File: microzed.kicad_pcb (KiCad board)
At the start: 10 copper layers, 50 x 100 mm, 334 parts, among them IC1 XC7Z020-1CLG484C, IC2 RTL8211E-VL-CG, J1 640456-3, J2 10104111-0001LF, J3 L829-1J1T-43, J4 Micro_SD_Card_Det_Hirose_DM3AT, J5 10104111-0001LF, J6 BSH-090-01-X-D-A, J7 BSH-090-01-X-D-A, Q1 MMBT3904, Q2 MMBT3904, SW1 SW_Push, U1 TLV62130RGTR, U10 MT41K256M16TW, U11 MT25QL128ABA8E12-1SIT, U12 USB3320C-EZK, U13 ASDMB-24.000MHZ-LC-T, U14 ASDMB-25.000MHZ-LC-T, U15 TXS02612RTWR, U16 CP2104-F03-GM, U2 TLV62130RGTR, U3 TLV62130RGTR, U4 TLV62130RGTR, U5 TLV62130RGTR, U6 ASDMB-33.333MHZ-LC-T, U7 TPS51206DSQR, U8 REF3012, U9 MT41K256M16TW

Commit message: pcb: start memory.
Signed-off-by: Yi Qingliang <niqingliang2003@gmail.com>
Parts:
- moved IC1 1.30 mm to (0.00, 48.2)
- moved U10 1.30 mm to (-5.40, 29.6)
- moved U9 1.30 mm to (5.40, 29.6)
- moved J6 1.30 mm to (-18.4, 45.0)
- moved J7 1.30 mm to (18.4, 45.0)
- moved C131 0.92 mm to (-7.40, 20.6), turned to 180 degrees
- moved C102 0.72 mm to (7.40, 20.6)
- moved C104 0.63 mm to (3.40, 20.6), turned to 180 degrees
- moved C121 0.61 mm to (-3.40, 20.6)
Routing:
- net DDR3_RST#: track 0.00 -> 0.57 mm, vias 0 -> 1
- net VCCO_DDR: vias 7 -> 13
- added copper zone on In5.Cu.GND, net VCCO_DDR

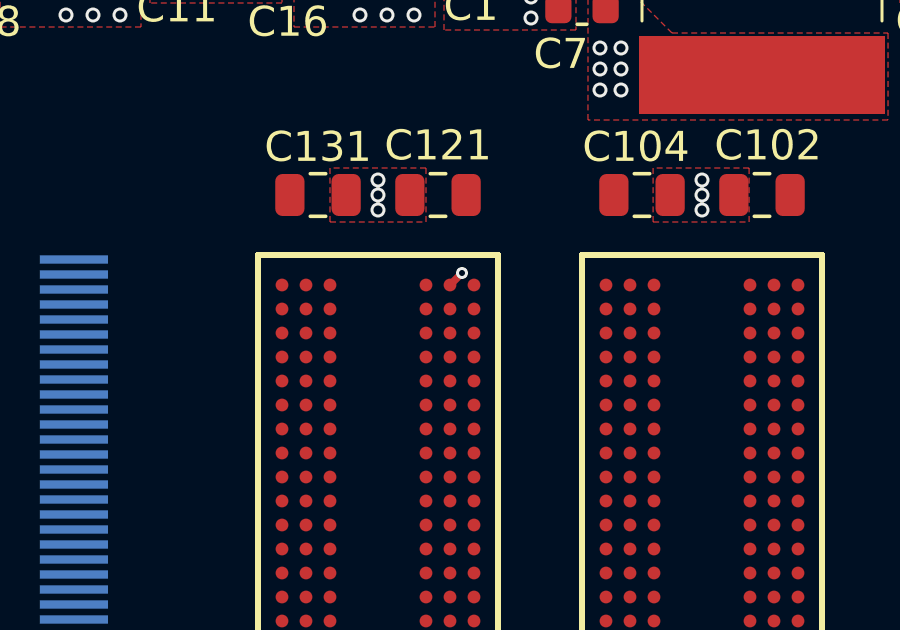
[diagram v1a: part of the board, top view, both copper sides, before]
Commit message: relax via settings
Signed-off-by: Yi Qingliang <niqingliang2003@gmail.com>
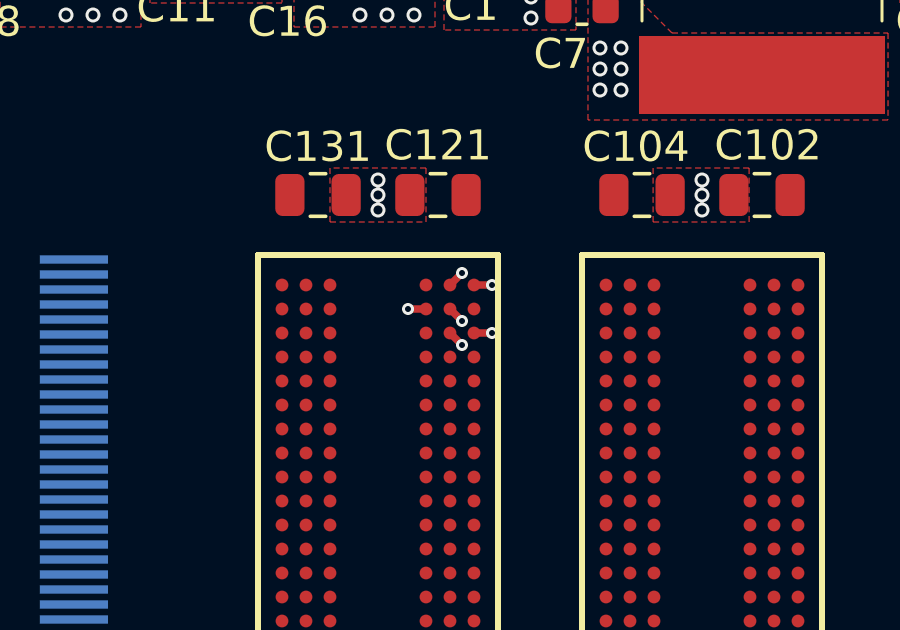
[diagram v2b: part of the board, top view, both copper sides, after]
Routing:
- net GND: track 16.4 -> 17.6 mm, vias 45 -> 47
- net DDR3_A9: track 0.00 -> 0.60 mm, vias 0 -> 1
- net DDR3_A7: track 0.00 -> 0.57 mm, vias 0 -> 1
- net DDR3_A5: track 0.00 -> 0.57 mm, vias 0 -> 1
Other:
- rule via_min_drill: 0.3 -> 0.2
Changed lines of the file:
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@@
     (thickness 1.6)
     (drawings 4)
-    (tracks 242)
+    (tracks 257)
     (zones 0)
     (modules 334)
@@
     (via_drill 0.4)
     (via_min_size 0.4)
-    (via_min_drill 0.3)
+    (via_min_drill 0.2)
+    (user_via 0.4 0.2)
     (user_via 0.5 0.3)
     (uvia_size 0.3)
@@
   (gr_line (start -25 100) (end -25 0) (layer Edge.Cuts) (width 0.05))
   (gr_line (start 25 100) (end -25 100) (layer Edge.Cuts) (width 0.05))
+  (via (at -2.6 25.6) (size 0.4) (drill 0.2) (layers F.Cu B.Cu) (net 222))
+  (via (at -2.6 24.8) (size 0.4) (drill 0.2) (layers F.Cu B.Cu) (net 234))
   (via (at -2.6 23.2) (size 0.4) (drill 0.2) (layers F.Cu B.Cu) (net 282))
-  (via (at -5.4 20.6) (size 0.5) (drill 0.3) (layers F.Cu B.Cu) (net 10))
-  (via (at -5.4 20.1) (size 0.5) (drill 0.3) (layers F.Cu B.Cu) (net 10))
-  (via (at -5.4 21.1) (size 0.5) (drill 0.3) (layers F.Cu B.Cu) (net 10))
   (via (at -18.3 10.5) (size 0.5) (drill 0.3) (layers F.Cu B.Cu) (net 1))
   (via (at -19.3 10.5) (size 0.5) (drill 0.3) (layers F.Cu B.Cu) (net 1))
@@
   (via (at 1.3 9.5) (size 0.5) (drill 0.3) (layers F.Cu B.Cu) (net 1))
   (via (at 0.8 10) (size 0.5) (drill 0.3) (layers F.Cu B.Cu) (net 1))
+  (segment (start -2.2 23.6) (end -1.6 23.6) (width 0.25) (layer F.Cu) (net 1))
+  (segment (start -1.6 23.6) (end -1.6 23.6) (width 0.25) (layer F.Cu) (net 1))
+  (segment (start -1.6 23.6) (end -1.6 23.6) (width 0.25) (layer F.Cu) (net 1))
+  (segment (start -2.2 25.2) (end -1.6 25.2) (width 0.25) (layer F.Cu) (net 1))
+  (segment (start -1.6 25.2) (end -1.6 25.2) (width 0.25) (layer F.Cu) (net 1))
+  (via (at -1.6 25.2) (size 0.4) (drill 0.2) (layers F.Cu B.Cu) (net 1))
+  (segment (start -1.6 23.6) (end -1.6 23.6) (width 0.25) (layer F.Cu) (net 1))
+  (via (at -1.6 23.6) (size 0.4) (drill 0.2) (layers F.Cu B.Cu) (net 1))
   (via (at 13.4 10) (size 0.5) (drill 0.3) (layers F.Cu B.Cu) (net 2))
   (via (at 12.4 10) (size 0.5) (drill 0.3) (layers F.Cu B.Cu) (net 2))
@@
   (segment (start 15.75 11.4625) (end 15.75 11.975) (width 0.25) (layer F.Cu) (net 9))
   (segment (start 15.75 11.975) (end 16.075 12.3) (width 0.25) (layer F.Cu) (net 9))
+  (via (at -5.4 20.6) (size 0.5) (drill 0.3) (layers F.Cu B.Cu) (net 10))
+  (via (at -5.4 20.1) (size 0.5) (drill 0.3) (layers F.Cu B.Cu) (net 10))
+  (via (at -5.4 21.1) (size 0.5) (drill 0.3) (layers F.Cu B.Cu) (net 10))
   (via (at -4.2 13.7) (size 0.5) (drill 0.3) (layers F.Cu B.Cu) (net 10))
   (via (at -6 13.7) (size 0.5) (drill 0.3) (layers F.Cu B.Cu) (net 10))
@@
   (via (at 5.4 20.1) (size 0.5) (drill 0.3) (layers F.Cu B.Cu) (net 10))
   (via (at 5.4 21.1) (size 0.5) (drill 0.3) (layers F.Cu B.Cu) (net 10))
+  (segment (start -3 25.2) (end -2.6 25.6) (width 0.25) (layer F.Cu) (net 222))
+  (segment (start -2.6 24.8) (end -3 24.4) (width 0.25) (layer F.Cu) (net 234))
+  (segment (start -3.8 24.4) (end -4.4 24.4) (width 0.25) (layer F.Cu) (net 246))
+  (segment (start -4.4 24.4) (end -4.4 24.4) (width 0.25) (layer F.Cu) (net 246))
+  (via (at -4.4 24.4) (size 0.4) (drill 0.2) (layers F.Cu B.Cu) (net 246))
   (segment (start -3 23.6) (end -2.6 23.2) (width 0.25) (layer F.Cu) (net 282))
   (via (at 18.7 8.8) (size 0.5) (drill 0.3) (layers F.Cu B.Cu) (net 350))

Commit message: start DDR3 DQ[0-7]
Signed-off-by: Yi Qingliang <niqingliang2003@gmail.com>
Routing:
- net DDR3_DQS0_P: track 0.00 -> 12.9 mm, vias 0 -> 2
- net DDR3_DQ5: track 0.00 -> 12.7 mm, vias 0 -> 2
- net DDR3_DQ1: track 0.00 -> 12.1 mm, vias 0 -> 2
- net DDR3_DQ3: track 0.00 -> 11.9 mm, vias 0 -> 2
- net DDR3_DQS0_N: track 0.00 -> 11.0 mm, vias 0 -> 2
- net DDR3_DQ7: track 0.00 -> 10.7 mm, vias 0 -> 2
- net DDR3_DQ2: track 0.00 -> 9.58 mm, vias 0 -> 2
- net DDR3_DQ0: track 0.00 -> 8.15 mm, vias 0 -> 2
- net GND: track 17.6 -> 19.3 mm, vias 47 -> 50
- net DDR3_A13: track 0.00 -> 1.17 mm, vias 0 -> 2
- net DDR3_DQ12: track 0.00 -> 1.15 mm, vias 0 -> 2
- net DDR3_DQ14: track 0.00 -> 1.13 mm, vias 0 -> 2
- net DDR3_DM0: track 0.00 -> 1.13 mm, vias 0 -> 2
- net DDR3_DQ9: track 0.00 -> 1.13 mm, vias 0 -> 2
- net DDR3_DQ15: track 0.00 -> 1.13 mm, vias 0 -> 2
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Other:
- net class DDRSignal added: clearance 0.1, trace_width 0.15, via_dia 0.4, via_drill 0.2
- net class Default: clearance 0.2 -> 0.1; via_dia 0.8 -> 0.5; via_drill 0.4 -> 0.3
- rule trace_clearance: 0.2 -> 0.1
- rule trace_min: 0.2 -> 0.15

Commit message: consider pin delay
Signed-off-by: Yi Qingliang <niqingliang2003@gmail.com>
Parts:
- removed the C5 at (-141.7, 328.3)
- moved U15 240.1 mm to (-77.2, 144.2)
- moved J4 232.7 mm to (-88.1, 134.3)
- moved C168 232.7 mm to (-76.7, 136.8)
- moved C169 232.7 mm to (-73.7, 134.8)
- moved C171 232.7 mm to (-76.7, 138.5)
- moved R97 232.7 mm to (-76.4, 134.9)
- moved C170 227.4 mm to (-78.0, 131.1)
- moved R99 227.4 mm to (-74.9, 127.2)
- moved R96 227.4 mm to (-77.8, 127.2)
- moved R98 227.4 mm to (-77.8, 129.2)
- moved C5 212.5 mm to (-66.0, 141.1)
- moved C181 209.9 mm to (-64.8, 144.5)
- moved R13 209.0 mm to (-57.4, 139.8)
- moved R7 208.6 mm to (-57.3, 142.8)
- moved C6 207.0 mm to (-58.9, 144.7)
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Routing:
- net DDR3_DQ11: track 1.13 -> 18.2 mm, vias 1 -> 3
- net DDR3_DQ13: track 1.13 -> 15.8 mm, vias 2 -> 4
- net DDR3_DQ5: track 12.7 -> 1.13 mm
- net DDR3_DM1: track 0.57 -> 11.8 mm, vias 1 -> 2
- net DDR3_DQ15: track 1.13 -> 12.1 mm
- net DDR3_DQ1: track 12.1 -> 1.17 mm
- net DDR3_DQ3: track 11.9 -> 1.13 mm
- net DDR3_DQ7: track 10.7 -> 1.17 mm
- net DDR3_DQ9: track 1.13 -> 10.4 mm
- net DDR3_DQ2: track 9.58 -> 1.13 mm
- net VCCO_DDR: track 12.8 -> 20.5 mm, vias 14 -> 27
- net GND: track 19.3 -> 27.0 mm, vias 50 -> 63
- net DDR3_DQ8: track 0.93 -> 8.38 mm, vias 2 -> 1
- net DDR3_DQS1_P: track 0.57 -> 8.00 mm, vias 1 -> 2
- net DDR3_DQS1_N: track 0.00 -> 7.37 mm, vias 0 -> 3
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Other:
- net class DDRSignal: trace_width 0.15 -> 0.1
- rule trace_min: 0.15 -> 0.1

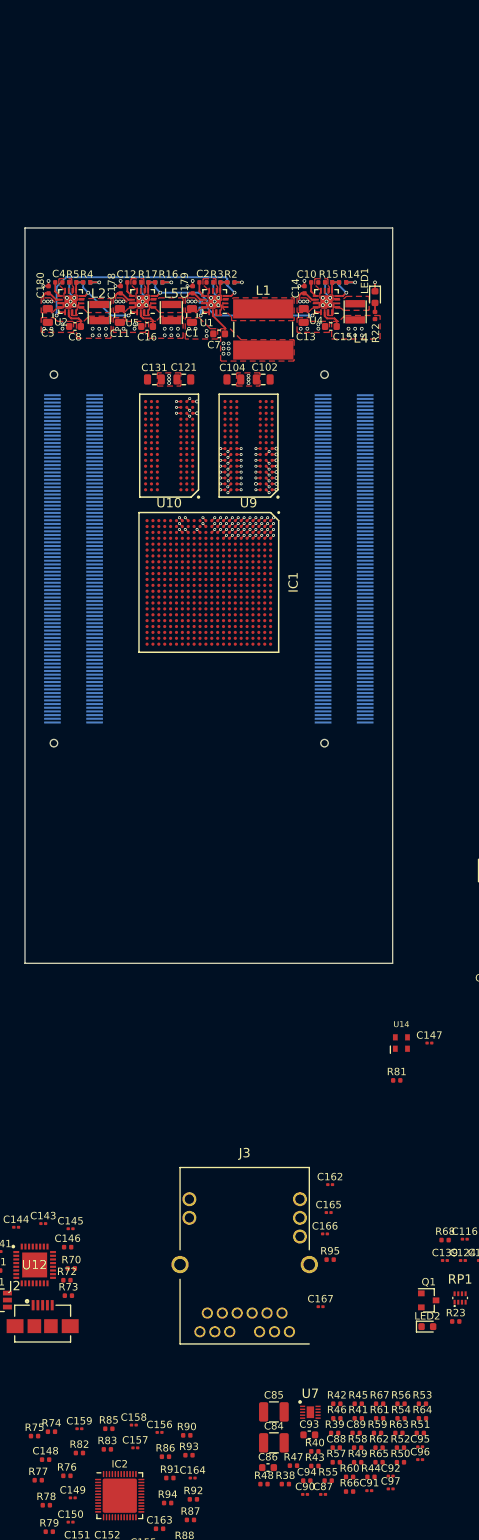
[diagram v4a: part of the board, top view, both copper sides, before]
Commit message: pcb: vtt power
Signed-off-by: Yi Qingliang <niqingliang2003@gmail.com>
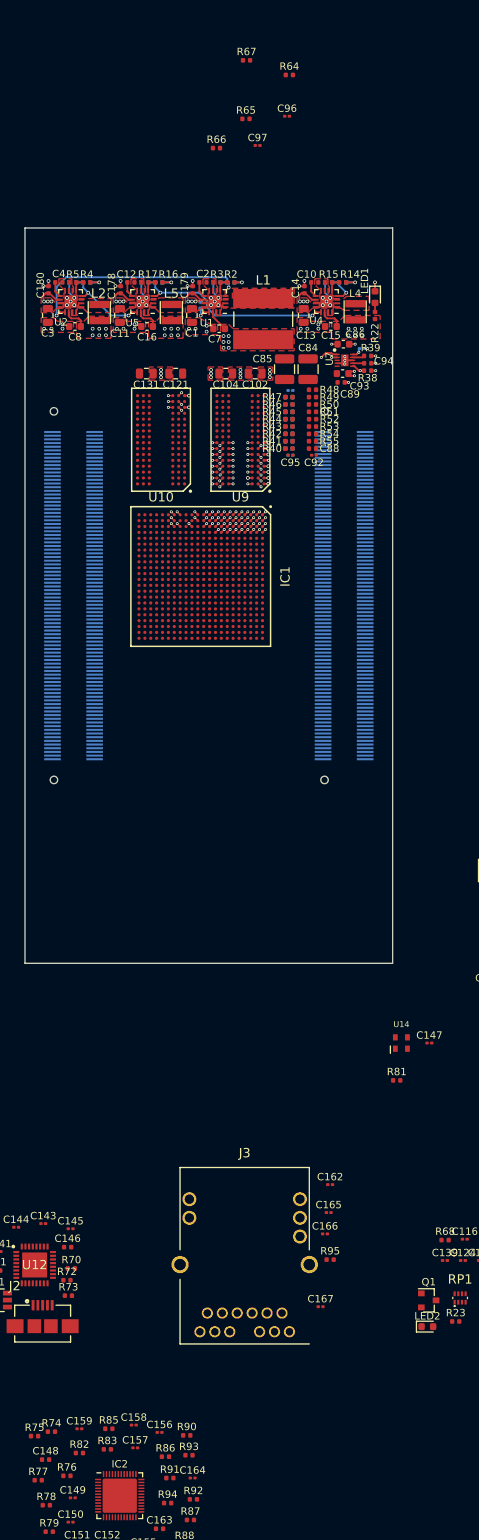
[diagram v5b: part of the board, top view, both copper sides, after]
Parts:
- C87, C90, C91, R56, R57, R58, R59, R60, R61, R62, R63: moved to B.Cu
- moved R65 183.6 mm to (5.05, -14.8)
- moved R67 183.6 mm to (5.13, -22.8)
- moved C96 183.6 mm to (10.6, -15.2)
- moved C97 183.6 mm to (6.63, -11.2)
- moved R64 183.6 mm to (10.9, -20.8)
- moved R66 183.6 mm to (1.04, -10.9)
- moved C87 155.9 mm to (20.8, 16.4)
- moved C86 153.1 mm to (18.3, 15.8)
- moved R38 152.8 mm to (21.6, 18.4)
- moved C94 151.2 mm to (21.6, 19.4)
- moved C90 150.1 mm to (11.1, 22.1), turned to 180 degrees
- moved R48 149.0 mm to (14.1, 22.0), turned to 180 degrees
- moved R39 146.5 mm to (21.6, 17.4)
- moved C84 146.1 mm to (13.5, 19.2), turned to 90 degrees
- moved R47 145.3 mm to (10.9, 23.0), turned to 180 degrees
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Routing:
- net GND: track 27.0 -> 33.5 mm, vias 63 -> 78
- net V3V3: track 12.9 -> 17.2 mm, vias 8 -> 13
- net VCCO_DDR: track 20.5 -> 22.9 mm, vias 27 -> 28
- net VTTREF: track 0.60 -> 2.41 mm, vias 1 -> 2
- net Net-(R39-Pad1): track 0.00 -> 1.65 mm
- net Net-(R38-Pad1): track 0.00 -> 1.56 mm
- net /pwrcvt/PG_1V: track 33.7 -> 32.6 mm
- net VCCBRAM: track 14.1 -> 13.0 mm

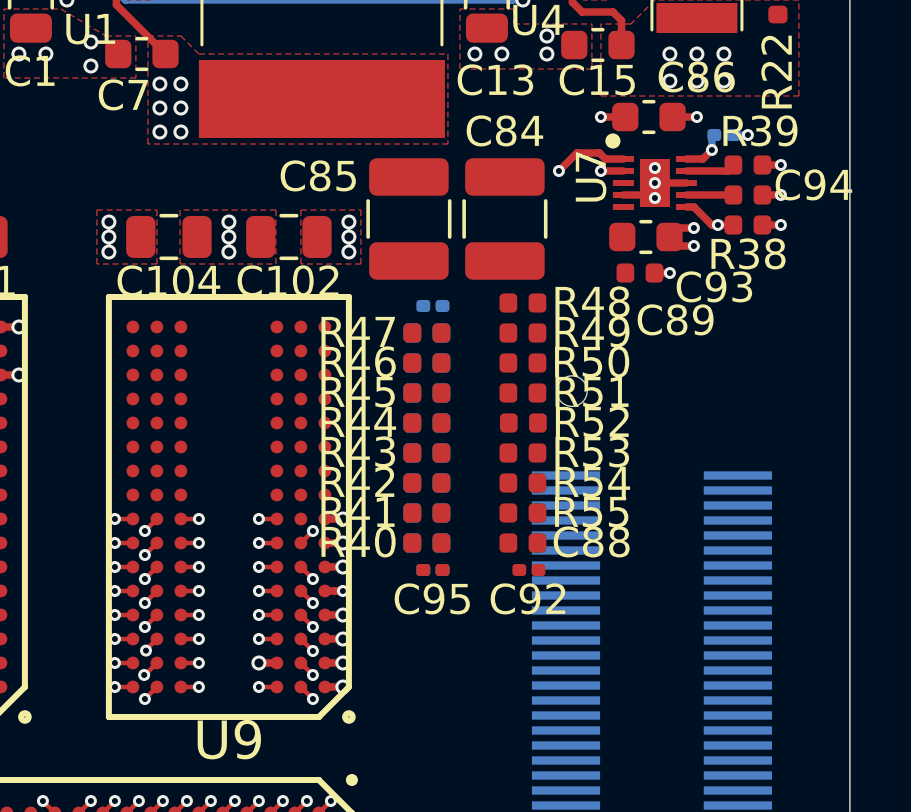
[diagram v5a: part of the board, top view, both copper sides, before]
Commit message: pcb: add terminate resistor for ddr3
Signed-off-by: Yi Qingliang <niqingliang2003@gmail.com>
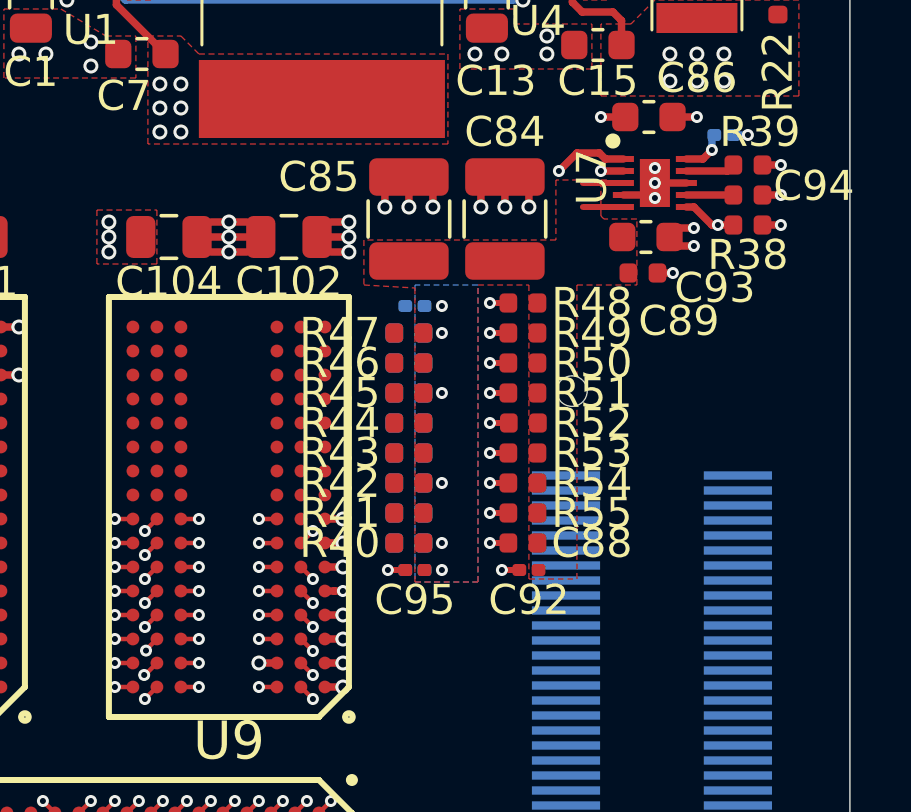
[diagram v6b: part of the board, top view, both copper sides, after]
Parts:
- moved C90 0.60 mm to (10.5, 22.1)
- moved C91 0.60 mm to (10.5, 30.9)
- moved C95 0.60 mm to (10.5, 30.9)
- moved R40 0.60 mm to (10.3, 30.0)
- moved R41 0.60 mm to (10.3, 29.0)
- moved R42 0.60 mm to (10.3, 28.0)
- moved R43 0.60 mm to (10.3, 27.0)
- moved R44 0.60 mm to (10.3, 26.0)
- moved R45 0.60 mm to (10.3, 25.0)
- moved R46 0.60 mm to (10.3, 24.0)
- moved R47 0.60 mm to (10.3, 23.0)
- moved R56 0.60 mm to (10.3, 30.0), turned to 180 degrees
- moved R57 0.60 mm to (10.3, 29.0), turned to 180 degrees
- moved R58 0.60 mm to (10.3, 28.0), turned to 180 degrees
- moved R59 0.60 mm to (10.3, 27.0), turned to 180 degrees
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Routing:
- net GND: track 33.5 -> 39.5 mm, vias 78 -> 87
- net VCCO_DDR: track 22.9 -> 26.5 mm
- net /BANK502/DDR3_VTT: track 0.00 -> 2.70 mm, vias 0 -> 6
- net DDR3_BA0: track 0.00 -> 0.62 mm, vias 0 -> 1
- net DDR3_A9: track 0.60 -> 1.21 mm, vias 1 -> 2
- net DDR3_A8: track 0.00 -> 0.62 mm, vias 0 -> 1
- net DDR3_A14: track 0.57 -> 1.18 mm, vias 1 -> 2
- net DDR3_A13: track 1.17 -> 1.78 mm, vias 2 -> 3
- net DDR3_A12: track 0.57 -> 1.18 mm, vias 1 -> 2
- net DDR3_A11: track 0.00 -> 0.62 mm, vias 0 -> 1
- net DDR3_A10: track 0.57 -> 1.18 mm, vias 1 -> 2
- added copper zone on B.Cu, net /BANK502/DDR3_VTT
- added copper zone on F.Cu, net /BANK502/DDR3_VTT

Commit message: continue memory capacitor
Signed-off-by: Yi Qingliang <niqingliang2003@gmail.com>
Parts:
- C120, C130, R65: moved to B.Cu
- moved SW1 195.5 mm to (58.4, 42.4)
- moved C130 120.5 mm to (-9.80, 24.9), turned to 90 degrees
- moved C120 116.3 mm to (8.60, 29.6), turned to 270 degrees
- moved C116 89.8 mm to (41.8, 48.0)
- moved C108 88.1 mm to (41.8, 43.4)
- moved C106 86.5 mm to (36.3, 42.8)
- moved C110 84.9 mm to (36.1, 45.4)
- moved C118 84.2 mm to (36.4, 51.4)
- moved C105 83.8 mm to (42.8, 56.8)
- moved C119 82.0 mm to (41.8, 50.2)
- moved C112 81.5 mm to (41.9, 45.5)
- moved C107 79.4 mm to (34.4, 58.1)
- moved C113 78.5 mm to (41.5, 61.5)
- moved C103 78.3 mm to (35.2, 55.4)
- moved C114 78.1 mm to (35.9, 48.7)
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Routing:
- net GND: track 39.5 -> 93.5 mm, vias 87 -> 171
- net VCCO_DDR: track 26.5 -> 46.8 mm, vias 28 -> 55
- net DDR3_DQ11: track 18.2 -> 1.13 mm, vias 3 -> 2
- net DDR3_DQ13: track 15.8 -> 1.13 mm, vias 4 -> 2
- net DDR3_DQS0_N: track 12.7 -> 1.16 mm
- net DDR3_DQ15: track 12.1 -> 1.17 mm
- net DDR3_DM1: track 11.8 -> 1.17 mm
- net DDR3_DQS0_P: track 11.0 -> 1.17 mm
- net DDR3_DQ9: track 10.4 -> 1.17 mm
- net VCCBRAM: track 13.0 -> 22.0 mm, vias 7 -> 23
- net PWR_B501: track 12.3 -> 19.7 mm, vias 7 -> 20
- net DDR3_DQ8: track 8.38 -> 1.17 mm, vias 1 -> 2
- net DDR3_DQ12: track 8.34 -> 1.17 mm, vias 1 -> 2
- net DDR3_DQS1_P: track 8.00 -> 1.17 mm
- net DDR3_DQ14: track 7.98 -> 1.16 mm
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- added copper zone on B.Cu, net VTTREF
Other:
- board size 50 x 100 mm -> 60 x 100 mm
- net class DDRSignal: clearance 0.1 -> 0.2; trace_width 0.1 -> 0.15
- net class Default: clearance 0.1 -> 0.2
- rule trace_clearance: 0.1 -> 0.2
